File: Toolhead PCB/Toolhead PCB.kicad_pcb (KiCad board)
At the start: 2 copper layers, 37.6 x 23.5 mm, 10 parts, among them J1 PicoA, J10 Conn_02x04_Odd_Even, J2 PicoB, J3 PicoC, J4 Heater, J5 Thermistor, J6 Heatbreak Fan, J7 Part Fan, J8 IR+ADXL345, J9 MicroProbe

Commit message: Shortened label on IR+ADXL345 --> IR/ADXL Set the IR/ADXL header to Do Not Populate, and Exclude from BOM
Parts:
- J8: value IR+ADXL345 -> IR/ADXL
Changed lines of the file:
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@@
 			)
 		)
-		(property "Value" "IR+ADXL345"
+		(property "Value" "IR/ADXL"
 			(at 8.725 0.09 0)
 			(layer "F.Fab")
@@
 		(sheetname "/")
 		(sheetfile "Toolhead PCB.kicad_sch")
-		(attr smd dnp)
+		(attr smd exclude_from_bom dnp)
 		(fp_line
 			(start -2.65 5.19)
@@
 		(sheetname "/")
 		(sheetfile "Toolhead PCB.kicad_sch")
-		(attr through_hole dnp)
+		(attr through_hole exclude_from_bom dnp)
 		(fp_line
 			(start -1.38 9)

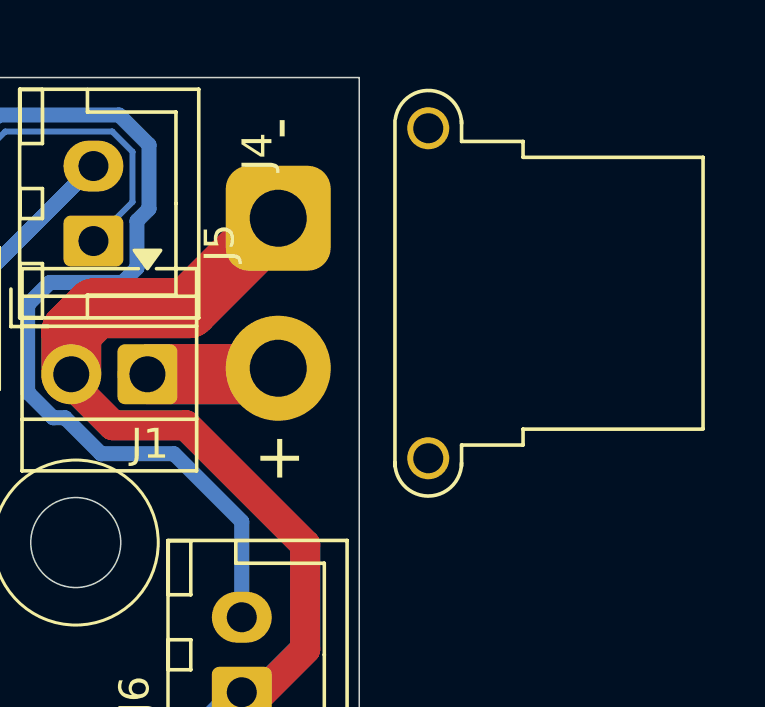
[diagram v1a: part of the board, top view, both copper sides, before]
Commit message: Changed XT30 footprint from `Connector_AMASS:AMASS_XT30PW-F_1x02_P2.50mm_Horizontal` to `Connector_AMASS:AMASS_XT30UPB-F_1x02_P5.0mm_Vertical` so there would not be the extra pads and drills for the connector supports which we do not use.
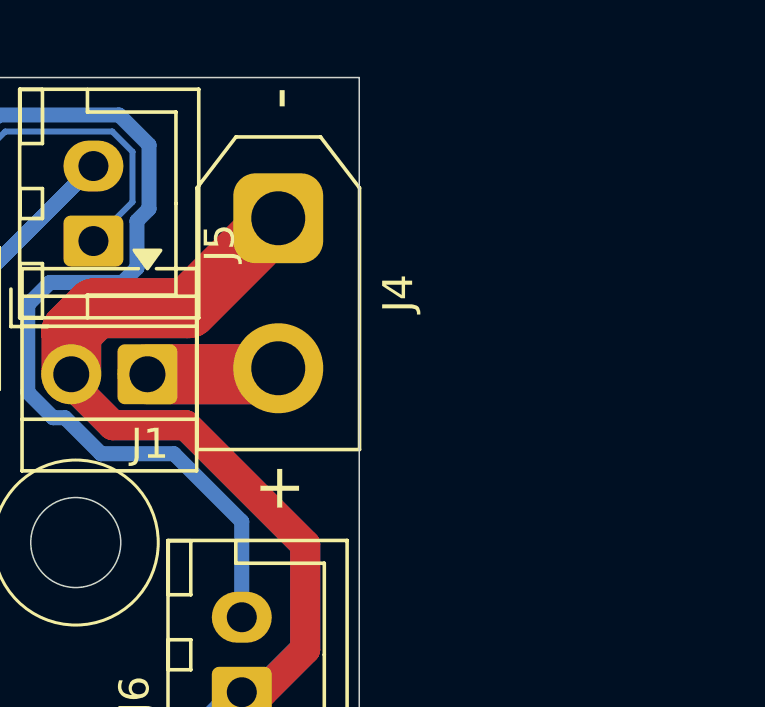
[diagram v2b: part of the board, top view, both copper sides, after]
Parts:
- J4: footprint Connector_AMASS:AMASS_XT30PW-F_1x02_P2.50mm_Horizontal -> Connector_AMASS:AMASS_XT30UPB-F_1x02_P5.0mm_Vertical
